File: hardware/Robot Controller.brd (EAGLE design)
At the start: 56.2 x 85.1 mm, 17 parts, among them U1 ATMEGA328P_PDIP

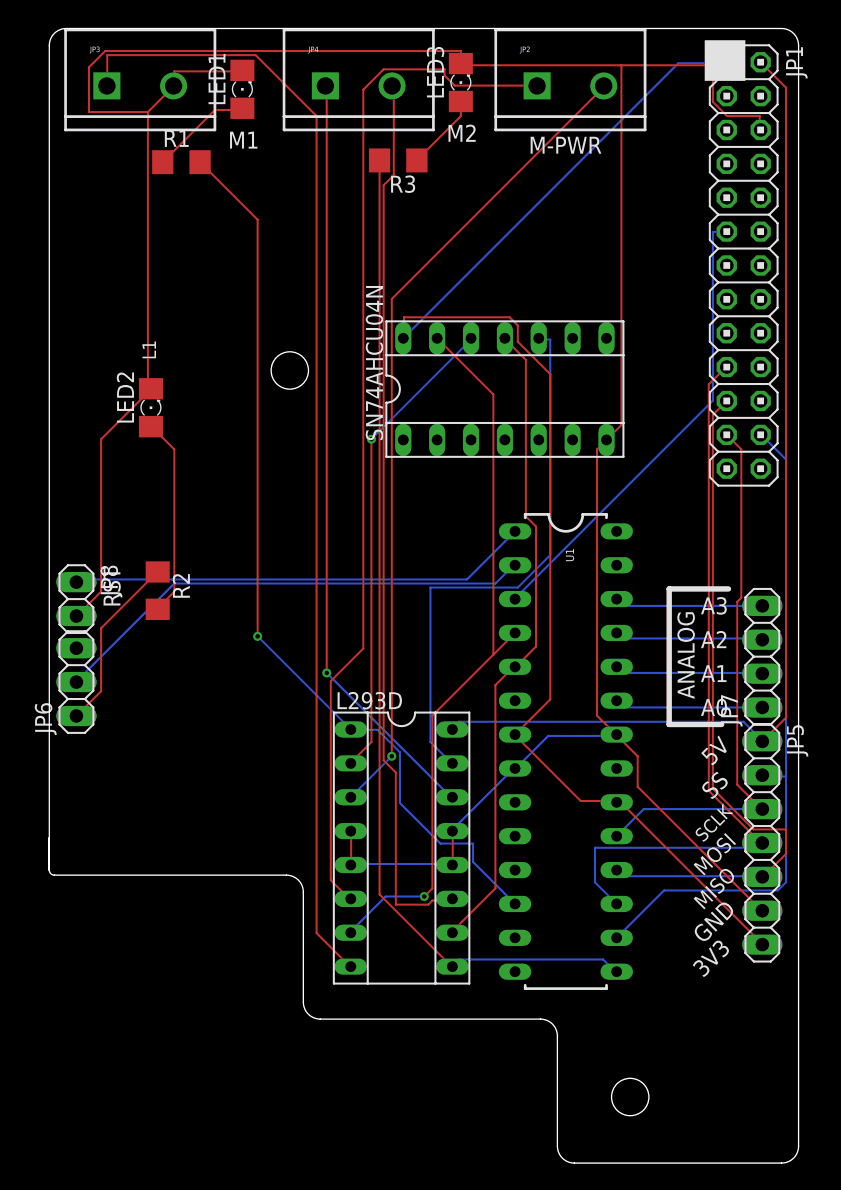
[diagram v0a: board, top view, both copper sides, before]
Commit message: fix outline
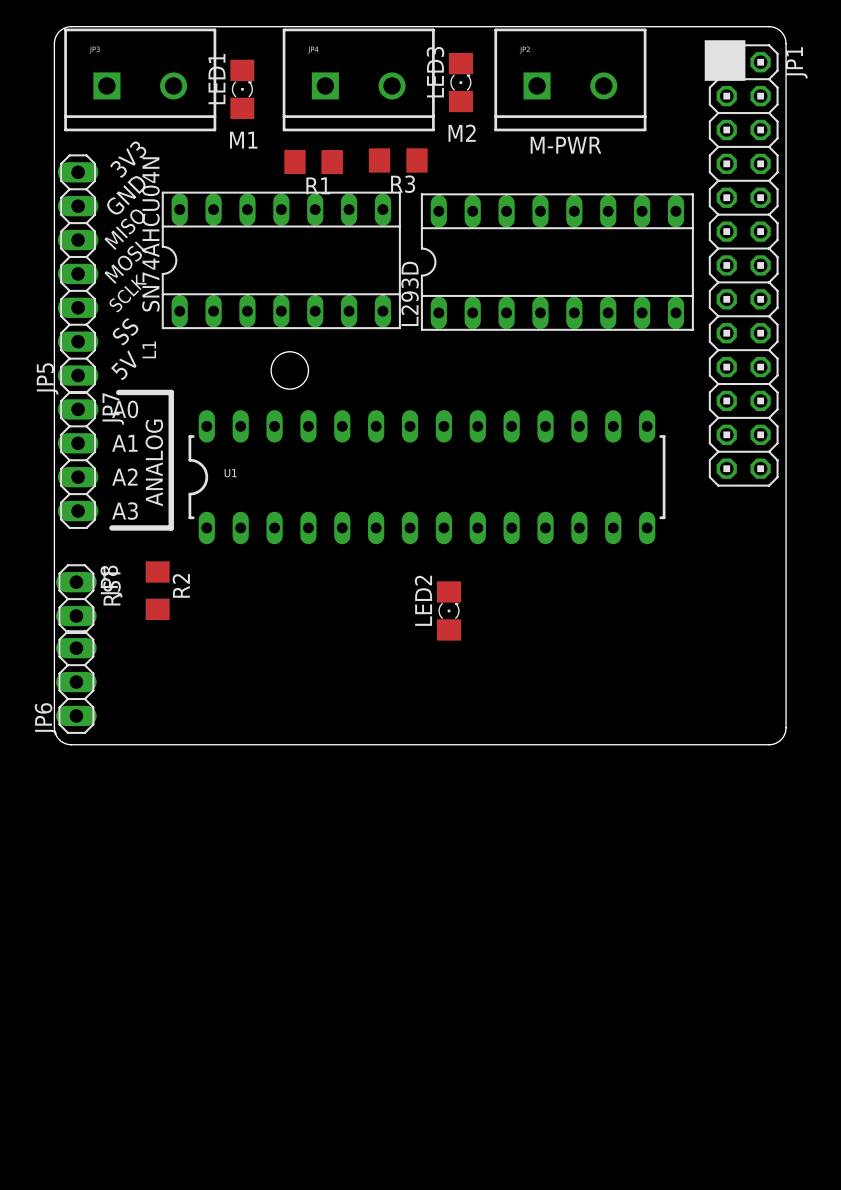
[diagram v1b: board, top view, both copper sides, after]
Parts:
- moved JP5 66.7 mm to (38.4, 54.6), turned to 90 degrees
- moved JP7 53.4 mm to (38.4, 40.6), turned to 270 degrees
- moved L293D 45.5 mm to (74.3, 55.5), turned to 0 degrees
- moved LED2 27.1 mm to (66.2, 29.3)
- moved U1 23.1 mm to (64.5, 39.4), turned to 0 degrees
- moved SN74AHCU04N 19.3 mm to (53.6, 55.6)
- moved R1 9.91 mm to (56.0, 63.0), turned to 180 degrees
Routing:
- net GND: track 211.2 -> 0.00 mm
- net 3.3V: track 101.1 -> 0.00 mm
- net N$10: track 84.8 -> 0.00 mm
- net N$9: track 76.8 -> 0.00 mm
- net 5V: track 76.6 -> 0.00 mm
- net M2PW: track 75.7 -> 0.00 mm
- net M1PW': track 68.0 -> 0.00 mm, vias 1 -> 0
- net N$19: track 66.6 -> 0.00 mm
- net N$8: track 61.2 -> 0.00 mm, vias 1 -> 0
- net N$18: track 57.3 -> 0.00 mm, vias 1 -> 0
- net MOSI': track 55.6 -> 0.00 mm
- net M1DR': track 54.7 -> 0.00 mm, vias 1 -> 0
- net MISO': track 51.7 -> 0.00 mm
- net SS': track 50.6 -> 0.00 mm
- net M2DR': track 48.2 -> 0.00 mm
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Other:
- board size 56.2 x 85.1 mm -> 54.9 x 53.8 mm
